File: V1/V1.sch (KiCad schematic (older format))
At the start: 40 parts, among them SW1 SW_Push, U1 ATmega32U4-AU, Y1 16MHz

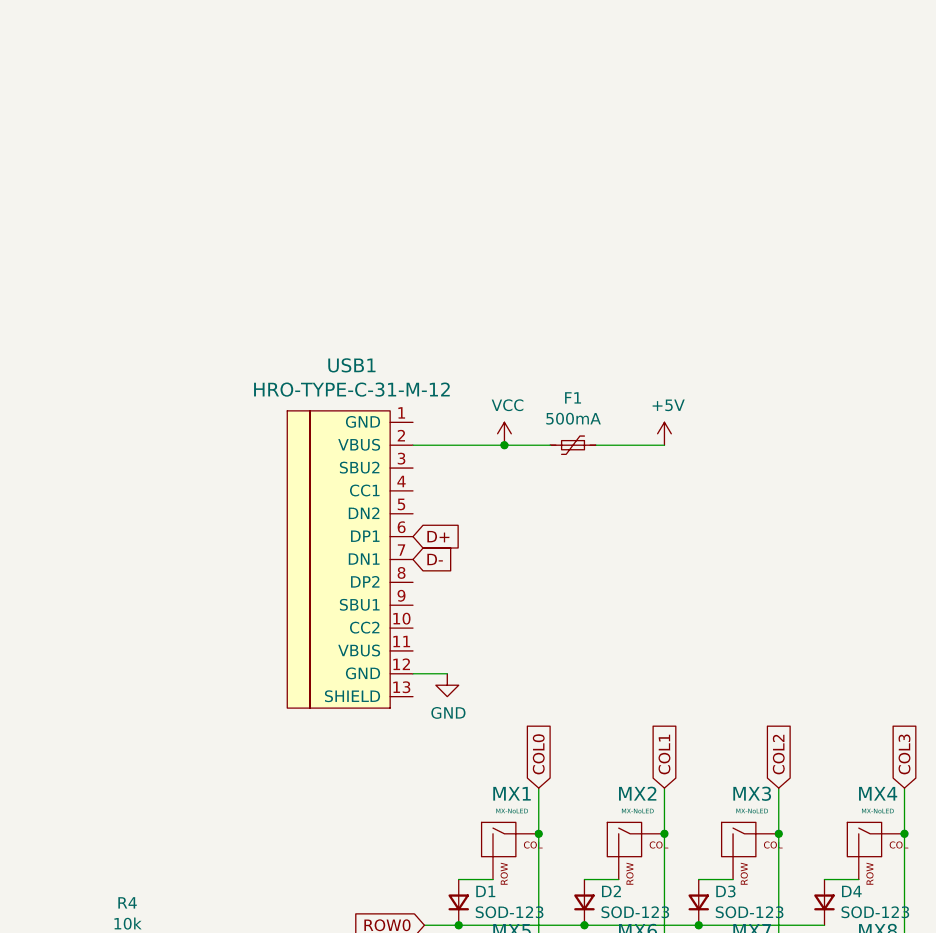
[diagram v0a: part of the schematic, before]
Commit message: Fixed Type C wiring
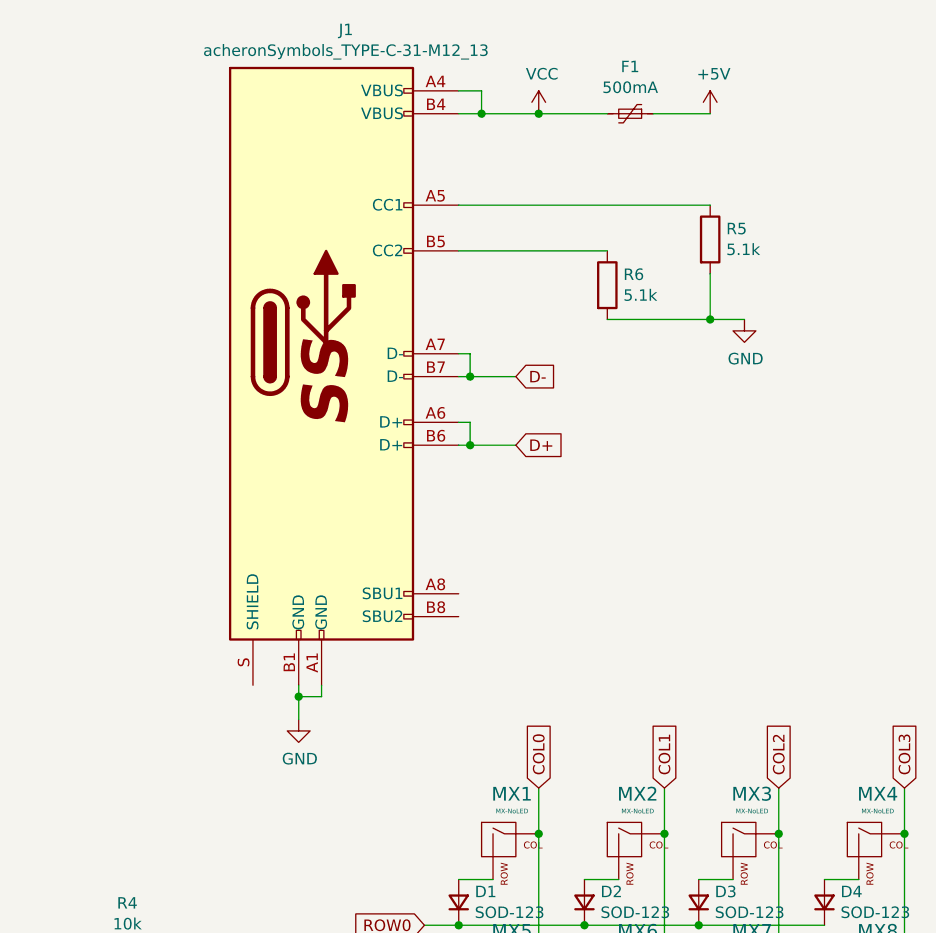
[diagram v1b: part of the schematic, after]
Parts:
- removed USB1: HRO-TYPE-C-31-M-12, Type-C:HRO-TYPE-C-31-M-12-Assembly, symbol Type-C:HRO-TYPE-C-31-M-12
- added J1: acheronSymbols_TYPE-C-31-M12_13, acheronConnectors:TYPE-C-31-M-12, symbol Unified-Daughterboard-cache:acheronSymbols_TYPE-C-31-M12_13
- added R5, R6: 5.1k, Resistor_SMD:R_0805_2012Metric, symbol Device:R
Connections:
- net D+: now also J1.A6 (D+), J1.B6 (D+)
- net D-: now also J1.A7 (D-), J1.B7 (D-)
- net GND: now also J1.A1 (GND), J1.B1 (GND), R5.2, R6.2
- net VCC: now also J1.A4 (VBUS), J1.B4 (VBUS)
- new net: J1.A5 (CC1), R5.1
- new net: J1.B5 (CC2), R6.1
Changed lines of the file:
@@
 Text GLabel 3400 3600 0    50   Input ~ 0
 D-
-$Comp
-L Type-C:HRO-TYPE-C-31-M-12 USB1
-U 1 1 618227A3
-P 7950 2850
-F 0 "USB1" H 7783 3647 60  0000 C CNN
-F 1 "HRO-TYPE-C-31-M-12" H 7783 3541 60  0000 C CNN
-F 2 "Type-C:HRO-TYPE-C-31-M-12-Assembly" H 7950 2850 60  0001 C CNN
-F 3 "" H 7950 2850 60  0001 C CNN
-	1    7950 2850
-	1    0    0    -1
-$EndComp
-$Comp
-L Device:Polyfuse_Small F1
-U 1 1 61826CB6
-P 8750 2400
-F 0 "F1" V 8545 2400 50  0000 C CNN
-F 1 "500mA" V 8636 2400 50  0000 C CNN
-F 2 "Fuse:Fuse_1206_3216Metric" H 8800 2200 50  0001 L CNN
-F 3 "~" H 8750 2400 50  0001 C CNN
-	1    8750 2400
-	0    1    1    0
-$EndComp
-$Comp
-L power:VCC #PWR0111
-U 1 1 6182BAC9
-P 8450 2400
-F 0 "#PWR0111" H 8450 2250 50  0001 C CNN
-F 1 "VCC" H 8465 2573 50  0000 C CNN
-F 2 "" H 8450 2400 50  0001 C CNN
-F 3 "" H 8450 2400 50  0001 C CNN
-	1    8450 2400
-	1    0    0    -1
-$EndComp
-Wire Wire Line
-	8050 2400 8450 2400
-Connection ~ 8450 2400
-Wire Wire Line
-	8450 2400 8650 2400
-$Comp
-L power:+5V #PWR0112
-U 1 1 6182DA7D
-P 9150 2400
-F 0 "#PWR0112" H 9150 2250 50  0001 C CNN
-F 1 "+5V" H 9165 2573 50  0000 C CNN
-F 2 "" H 9150 2400 50  0001 C CNN
-F 3 "" H 9150 2400 50  0001 C CNN
-	1    9150 2400
-	1    0    0    -1
-$EndComp
-Wire Wire Line
-	8850 2400 9150 2400
-Text GLabel 8050 2800 2    50   Input ~ 0
-D+
-Text GLabel 8050 2900 2    50   Input ~ 0
-D-
-Wire Wire Line
-	8050 3400 8200 3400
 Wire Wire Line
 	8800 4300 8950 4300
@@
 F 3 "" H 7825 4125 60  0001 C CNN
 	1    8450 4150
-	1    0    0    -1
-$EndComp
-$Comp
-L power:GND #PWR0113
-U 1 1 61832211
-P 8200 3400
-F 0 "#PWR0113" H 8200 3150 50  0001 C CNN
-F 1 "GND" H 8205 3227 50  0000 C CNN
-F 2 "" H 8200 3400 50  0001 C CNN
-F 3 "" H 8200 3400 50  0001 C CNN
-	1    8200 3400
 	1    0    0    -1
 $EndComp
@@
 Text GLabel 10200 3900 1    50   Input ~ 0
 COL3
+$Comp
+L Unified-Daughterboard-cache:acheronSymbols_TYPE-C-31-M12_13 J1
+U 1 1 61804EB1
+P 7650 2000
+F 0 "J1" H 7757 3417 50  0000 C CNN
+F 1 "acheronSymbols_TYPE-C-31-M12_13" H 7757 3326 50  0000 C CNN
+F 2 "acheronConnectors:TYPE-C-31-M-12" V 7150 2050 50  0001 C CNN
+F 3 "" H 7850 2050 50  0001 C CNN
+	1    7650 2000
+	1    0    0    -1
+$EndComp
+Wire Wire Line
+	8250 950  8350 950
+Wire Wire Line
+	8250 850  8350 850
+Wire Wire Line
+	8350 850  8350 950
+Connection ~ 8350 950
+Wire Wire Line
+	8350 950  8600 950
+$Comp
+L power:VCC #PWR0111
+U 1 1 6183E869
+P 8600 950
+F 0 "#PWR0111" H 8600 800 50  0001 C CNN
+F 1 "VCC" H 8615 1123 50  0000 C CNN
+F 2 "" H 8600 950 50  0001 C CNN
+F 3 "" H 8600 950 50  0001 C CNN
+	1    8600 950
+	1    0    0    -1
+$EndComp
+$Comp
+L Device:Polyfuse_Small F1
+U 1 1 6183FB82
+P 9000 950
+F 0 "F1" V 8795 950 50  0000 C CNN
+F 1 "500mA" V 8886 950 50  0000 C CNN
+F 2 "Fuse:Fuse_1206_3216Metric" H 9050 750 50  0001 L CNN
+F 3 "~" H 9000 950 50  0001 C CNN
+	1    9000 950
+	0    1    1    0
+$EndComp
+Wire Wire Line
+	8600 950  8900 950
+Connection ~ 8600 950
+Wire Wire Line
+	9100 950  9350 950
+$Comp
+L power:+5V #PWR0112
+U 1 1 618452D0
+P 9350 950
+F 0 "#PWR0112" H 9350 800 50  0001 C CNN
+F 1 "+5V" H 9365 1123 50  0000 C CNN
+F 2 "" H 9350 950 50  0001 C CNN
+F 3 "" H 9350 950 50  0001 C CNN
+	1    9350 950
+	1    0    0    -1
+$EndComp
+Wire Wire Line
+	8250 2100 8300 2100
+Wire Wire Line
+	8250 2000 8300 2000
+Wire Wire Line
+	8300 2000 8300 2100
+Connection ~ 8300 2100
+Wire Wire Line
+	8300 2100 8500 2100
+Wire Wire Line
+	8250 2400 8300 2400
+Wire Wire Line
+	8250 2300 8300 2300
+Wire Wire Line
+	8300 2300 8300 2400
+Connection ~ 8300 2400
+Wire Wire Line
+	8300 2400 8500 2400
+Wire Wire Line
+	7550 3450 7550 3500
+Wire Wire Line
+	7650 3450 7650 3500
+Wire Wire Line
+	7650 3500 7550 3500
+Connection ~ 7550 3500
+Wire Wire Line
+	7550 3500 7550 3600
+$Comp
+L power:GND #PWR0113
+U 1 1 618653CC
+P 7550 3600
+F 0 "#PWR0113" H 7550 3350 50  0001 C CNN
+F 1 "GND" H 7555 3427 50  0000 C CNN
+F 2 "" H 7550 3600 50  0001 C CNN
+F 3 "" H 7550 3600 50  0001 C CNN
+	1    7550 3600
+	1    0    0    -1
+$EndComp
+Text GLabel 8500 2100 2    50   Input ~ 0
+D-
+Text GLabel 8500 2400 2    50   Input ~ 0
+D+
+Wire Wire Line
+	8250 1350 9350 1350
+Wire Wire Line
+	8250 1550 8900 1550
+$Comp
+L Device:R R6
+U 1 1 6186EFA0
+P 8900 1700
+F 0 "R6" H 8970 1746 50  0000 L CNN
+F 1 "5.1k" H 8970 1655 50  0000 L CNN
+F 2 "Resistor_SMD:R_0805_2012Metric" V 8830 1700 50  0001 C CNN
+F 3 "~" H 8900 1700 50  0001 C CNN
+	1    8900 1700
+	1    0    0    -1
+$EndComp
+$Comp
+L Device:R R5
+U 1 1 6187320B
+P 9350 1500
+F 0 "R5" H 9420 1546 50  0000 L CNN
+F 1 "5.1k" H 9420 1455 50  0000 L CNN
+F 2 "Resistor_SMD:R_0805_2012Metric" V 9280 1500 50  0001 C CNN
+F 3 "~" H 9350 1500 50  0001 C CNN
+	1    9350 1500
+	1    0    0    -1
+$EndComp
+Wire Wire Line
+	8900 1850 9350 1850
+Wire Wire Line
+	9350 1650 9350 1850
+Connection ~ 9350 1850
+Wire Wire Line
+	9350 1850 9500 1850
+$Comp
+L power:GND #PWR0114
+U 1 1 6187AC07
+P 9500 1850
+F 0 "#PWR0114" H 9500 1600 50  0001 C CNN
+F 1 "GND" H 9505 1677 50  0000 C CNN
+F 2 "" H 9500 1850 50  0001 C CNN
+F 3 "" H 9500 1850 50  0001 C CNN
+	1    9500 1850
+	1    0    0    -1
+$EndComp
 $EndSCHEMATC
